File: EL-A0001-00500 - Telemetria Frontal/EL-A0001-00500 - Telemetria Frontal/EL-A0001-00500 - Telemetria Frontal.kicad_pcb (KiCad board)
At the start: 2 copper layers, 40 parts, among them J1 1-776087-1, J2 Conn_01x02_Male, J3 Conn_01x04_Male, J4 Conn_01x04_Male, J5 UART, J6 Conn_01x04_Male, U1 YAAJ_BluePill, U2 MP1584, U3 LM324, U4 LM324, U5 TJA1050-Module

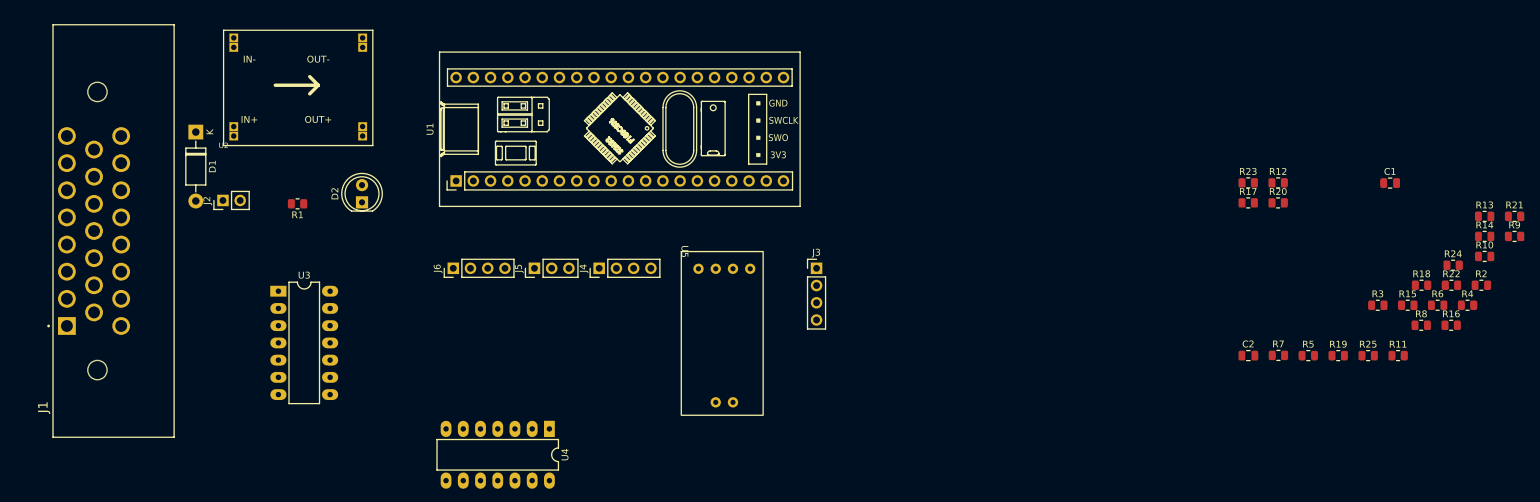
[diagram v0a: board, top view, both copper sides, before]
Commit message: ADD: fusiveis BMS
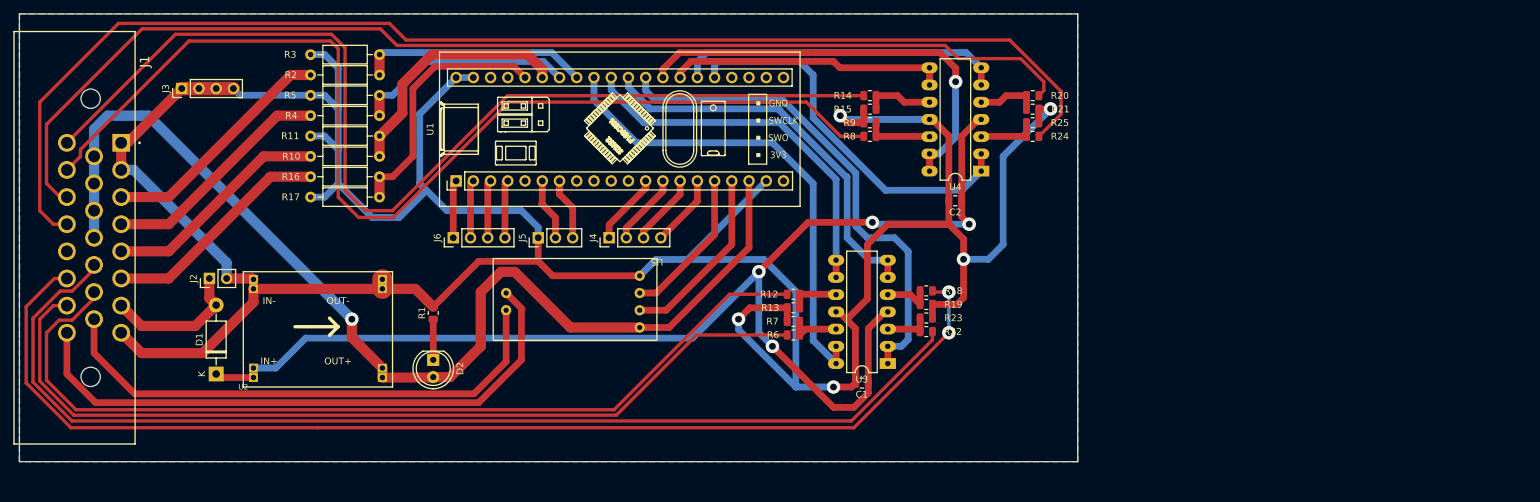
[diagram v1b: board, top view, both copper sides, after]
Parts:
- R10, R11, R16, R17, R2, R3, R4, R5: footprint Resistor_SMD:R_0805_2012Metric -> Resistor_THT:R_Axial_DIN0207_L6.3mm_D2.5mm_P10.16mm_Horizontal
- U2: footprint MP1584:DC-BRICK -> Cheetah:DC-BRICK
- moved R2 165.4 mm to (78.1, 48.0), turned to 180 degrees
- moved R10 163.6 mm to (78.1, 60.0), turned to 180 degrees
- moved R11 163.5 mm to (67.9, 57.0)
- moved R4 162.8 mm to (78.1, 54.0), turned to 180 degrees
- moved R3 161.6 mm to (67.9, 45.0)
- moved R16 159.5 mm to (78.1, 63.0), turned to 180 degrees
- moved R5 152.0 mm to (67.9, 51.0)
- moved R17 138.2 mm to (67.9, 66.0)
- moved R13 102.8 mm to (139.1, 82.3)
- moved J3 97.3 mm to (48.9, 50.0), turned to 90 degrees
- moved R9 96.5 mm to (150.4, 55.0)
- moved R6 95.1 mm to (139.1, 86.3), turned to 180 degrees
- moved R14 93.0 mm to (150.4, 51.0), turned to 180 degrees
- moved U3 90.5 mm to (153.0, 90.5), turned to 180 degrees
- moved R8 85.9 mm to (150.4, 57.0), turned to 180 degrees
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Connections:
- C1 pad 1: Net-(U2-PadIN1+) -> Net-(C1-Pad1)
- C2 pad 1: Net-(U2-PadIN1+) -> Net-(C1-Pad1)
- D1 pad 1: Net-(U2-PadIN1+) -> Net-(C1-Pad1)
- D1 pad 2: Net-(D1-Pad2) -> VIN
- J1 pad 1: unconnected-(J1-Pad1) -> GNDREF
- J1 pad 10: unconnected-(J1-Pad10) -> +5V
- J1 pad 11: unconnected-(J1-Pad11) -> +5V
- J1 pad 12: unconnected-(J1-Pad12) -> +5V
- J1 pad 13: unconnected-(J1-Pad13) -> PRESSURE_3
- J1 pad 14: unconnected-(J1-Pad14) -> ADC_1
- J1 pad 15: unconnected-(J1-Pad15) -> CANH
- J1 pad 16: unconnected-(J1-Pad16) -> PRESSURE_1
- J1 pad 17: unconnected-(J1-Pad17) -> PRESSURE_2
- J1 pad 18: unconnected-(J1-Pad18) -> TPS_2
- J1 pad 19: unconnected-(J1-Pad19) -> TPS_1
- J1 pad 2: unconnected-(J1-Pad2) -> GNDREF
- J1 pad 21: unconnected-(J1-Pad21) -> ENCODER
- J1 pad 22: unconnected-(J1-Pad22) -> ADC_2
- J1 pad 23: unconnected-(J1-Pad23) -> CANL
- J1 pad 3: unconnected-(J1-Pad3) -> DI_1
- J1 pad 4: unconnected-(J1-Pad4) -> DI_2
- J1 pad 5: unconnected-(J1-Pad5) -> DI_3
- J1 pad 6: unconnected-(J1-Pad6) -> DI_4
- J1 pad 7: unconnected-(J1-Pad7) -> VIN
- J1 pad 8: unconnected-(J1-Pad8) -> GNDREF
- J1 pad 9: unconnected-(J1-Pad9) -> +5V
- J2 pad 1: Net-(D1-Pad2) -> VIN
- U3 pad 4: Net-(U2-PadIN1+) -> Net-(C1-Pad1)
- U4 pad 4: Net-(U2-PadIN1+) -> Net-(C1-Pad1)
- U5 pad 5: unconnected-(U5-Pad5) -> CANH
- U5 pad 6: unconnected-(U5-Pad6) -> CANL
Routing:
- net GNDREF: track 0.00 -> 466.5 mm, vias 0 -> 5
- net TPS_1: track 0.00 -> 188.3 mm
- net Net-(C1-Pad1): track 0.00 -> 182.9 mm, vias 0 -> 4
- net ENCODER: track 0.00 -> 172.0 mm, vias 0 -> 2
- net TPS_2: track 0.00 -> 171.0 mm
- net PRESSURE_3: track 0.00 -> 163.2 mm
- net +5V: track 0.00 -> 161.0 mm, vias 0 -> 1
- net PRESSURE_2: track 0.00 -> 158.6 mm
- net PRESSURE_1: track 0.00 -> 154.2 mm
- net ADC_1: track 0.00 -> 135.0 mm
- net ADC_2: track 0.00 -> 131.1 mm
- net CANL: track 0.00 -> 88.2 mm
- net CANH: track 0.00 -> 77.8 mm
- net Net-(U1-Pad29): track 0.00 -> 74.0 mm
- net Net-(U1-Pad32): track 0.00 -> 71.2 mm
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- added copper zone on B.Cu, net GNDREF
- added copper zone on F.Cu, net GNDREF
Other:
- board outline added: 156 x 66 mm
